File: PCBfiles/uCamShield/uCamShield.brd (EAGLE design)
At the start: 81.5 x 53.3 mm, 9 parts

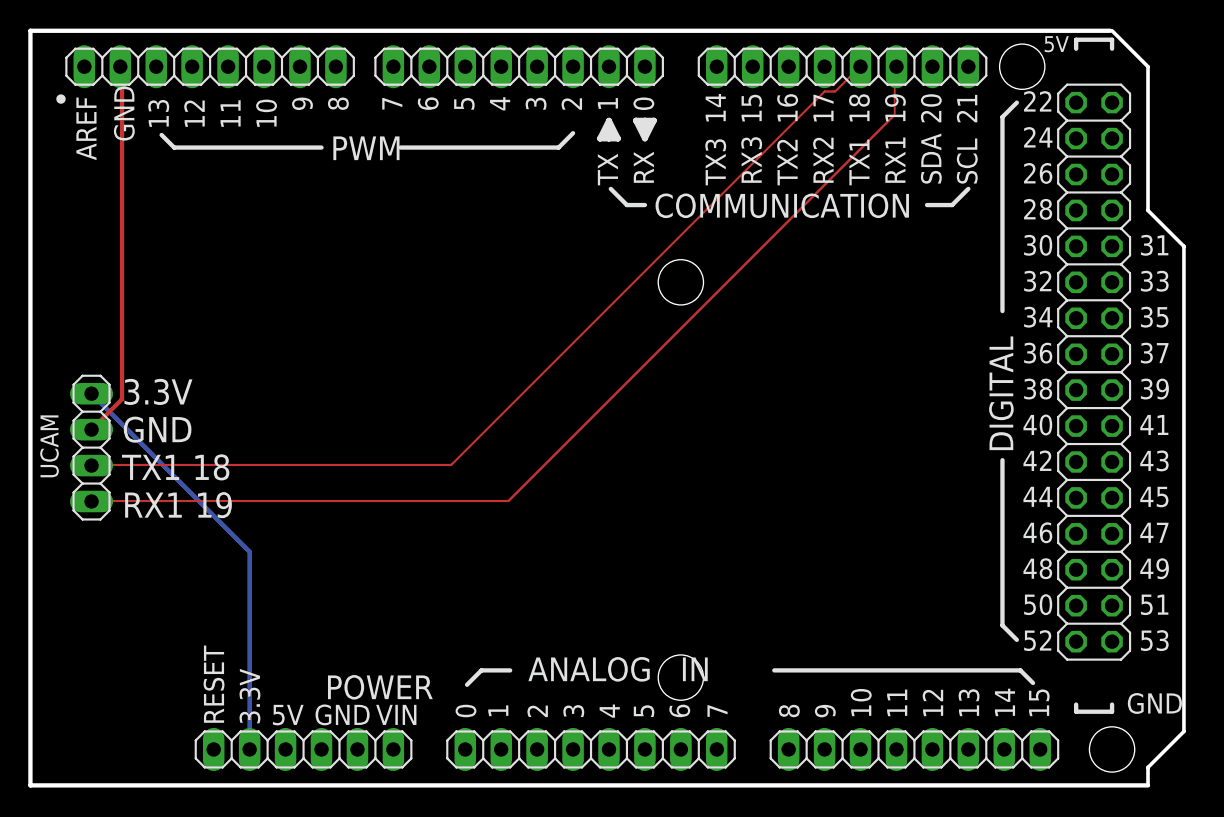
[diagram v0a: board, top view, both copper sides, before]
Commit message: Fixed PCB file for uCam shield
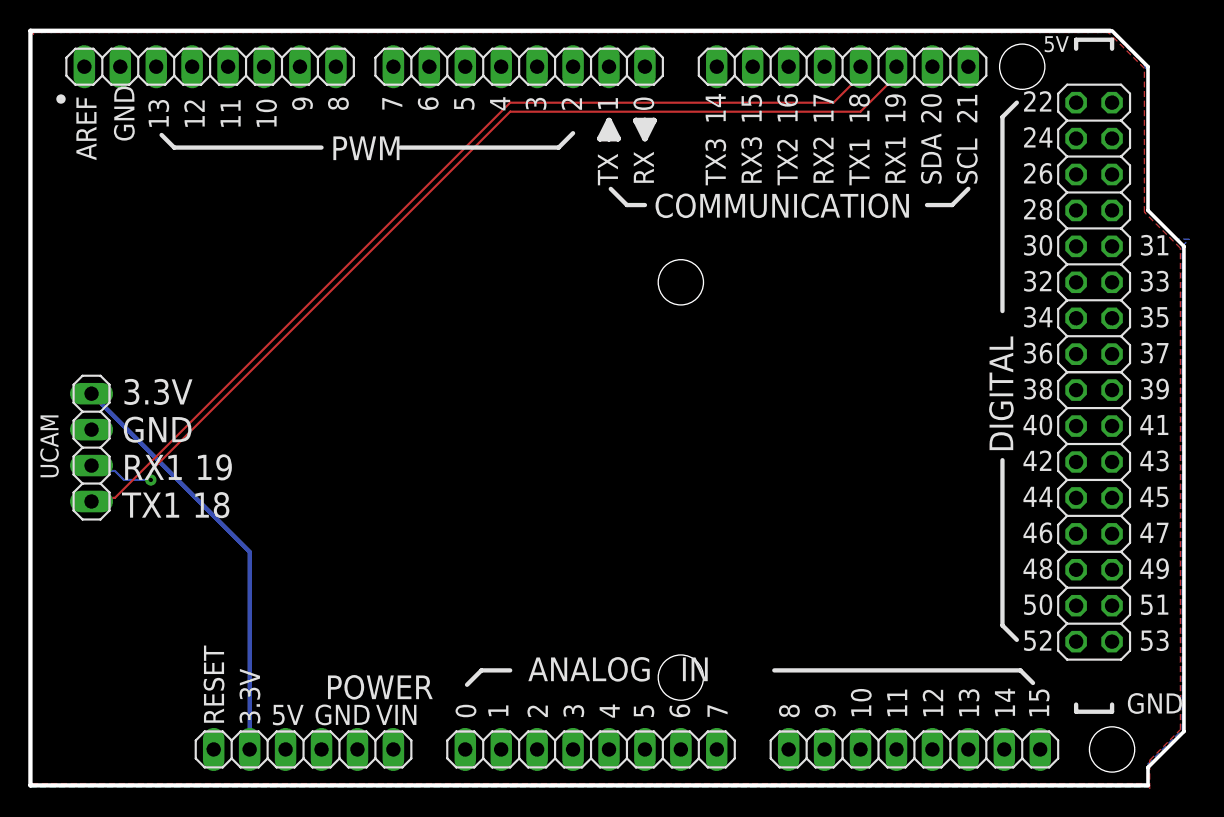
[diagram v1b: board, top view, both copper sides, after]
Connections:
- removed net N$4: COMMUNICATION.3, UCAM.1
- new net GND: POWER.4, POWER.5, PWMH.7, UCAM.3
- net N$2: now also COMMUNICATION.4, UCAM.1; no longer PWMH.7, UCAM.3
- net N$3: now also COMMUNICATION.3; no longer COMMUNICATION.4
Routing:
- net N$4: track 71.5 -> 0.00 mm
- net N$2: track 26.6 -> 67.4 mm
- net N$3: track 66.0 -> 70.2 mm, vias 0 -> 1
- added copper zone on layer 1, net GND
- added copper zone on layer 16, net GND
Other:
- board text added: "3.3V GND RX1 19 TX1 18"
- board text added: "uCAM-ARD-SHD rev0.2"
- board text removed: "3.3V GND TX1 18 RX1 19"
- board text removed: "uCAM-ARD-SHD rev.1"
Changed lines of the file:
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@@
 <text x="26.543" y="18.923" size="1.778" layer="21">3.3V
 GND
-TX1 18
-RX1 19</text>
+RX1 19
+TX1 18</text>
 <wire x1="96.393" y1="53.34" x2="20.066" y2="53.34" width="0.3048" layer="20"/>
 <wire x1="20.066" y1="53.34" x2="20.066" y2="0" width="0.3048" layer="20"/>
 <wire x1="20.066" y1="0" x2="99.06" y2="0" width="0.3048" layer="20"/>
 <text x="81.915" y="24.257" size="1.778" layer="22" rot="MR0">uCAM-ARD-SHD
-rev.1</text>
+rev0.2</text>
+<polygon width="0.4064" layer="22">
+<vertex x="43.688" y="31.242"/>
+<vertex x="41.021" y="31.242"/>
+<vertex x="38.227" y="28.448"/>
+<vertex x="38.227" y="19.558"/>
+<vertex x="39.878" y="19.558"/>
+<vertex x="40.005" y="19.685"/>
+<vertex x="40.005" y="27.94"/>
+<vertex x="41.656" y="29.591"/>
+<vertex x="43.815" y="29.591"/>
+<vertex x="45.212" y="28.194"/>
+<vertex x="45.212" y="19.558"/>
+<vertex x="45.085" y="19.431"/>
+<vertex x="47.117" y="19.431"/>
+<vertex x="47.117" y="28.067"/>
+<vertex x="44.069" y="31.115"/>
+</polygon>
+<polygon width="0.4064" layer="22">
+<vertex x="40.259" y="25.273"/>
+<vertex x="44.958" y="25.273"/>
+<vertex x="44.958" y="23.622"/>
+<vertex x="39.878" y="23.622"/>
+<vertex x="39.878" y="23.495"/>
+<vertex x="40.005" y="23.495"/>
+<vertex x="40.005" y="24.13"/>
+</polygon>
 </plain>
 <attributes>
@@
 <param name="RoutingGrid" value="50mil"/>
 <param name="AutoGrid" value="1"/>
-<param name="Efforts" value="0"/>
+<param name="Efforts" value="2"/>
 <param name="TopRouterVariant" value="1"/>
 <param name="tpViaShape" value="round"/>
-<param name="PrefDir.1" value="|"/>
+<param name="PrefDir.1" value="a"/>
 <param name="PrefDir.2" value="0"/>
 <param name="PrefDir.3" value="0"/>
@@
 <param name="PrefDir.14" value="0"/>
 <param name="PrefDir.15" value="0"/>
-<param name="PrefDir.16" value="-"/>
+<param name="PrefDir.16" value="a"/>
 <param name="cfVia" value="8"/>
 <param name="cfNonPref" value="5"/>
@@
 <wire x1="35.55" y1="3.45" x2="35.56" y2="3.556" width="0.15" layer="16"/>
 </signal>
+<signal name="GND">
+<contactref element="PWMH" pad="7"/>
+<contactref element="UCAM" pad="3"/>
+<contactref element="POWER" pad="4"/>
+<contactref element="POWER" pad="5"/>
+<polygon width="0.4064" layer="16">
+<vertex x="20.066" y="53.34"/>
+<vertex x="20.066" y="-0.127"/>
+<vertex x="98.933" y="-0.127"/>
+<vertex x="99.06" y="0"/>
+<vertex x="99.06" y="1.143"/>
+<vertex x="99.06" y="1.524"/>
+<vertex x="101.473" y="3.937"/>
+<vertex x="101.473" y="38.1"/>
+<vertex x="101.981" y="38.608"/>
+<vertex x="101.092" y="38.608"/>
+<vertex x="99.06" y="40.64"/>
+<vertex x="99.06" y="50.546"/>
+<vertex x="98.806" y="50.8"/>
+<vertex x="98.806" y="50.927"/>
+<vertex x="96.52" y="53.213"/>
+<vertex x="20.193" y="53.213"/>
+</polygon>
+<polygon width="0.4064" layer="1">
+<vertex x="20.066" y="53.213"/>
+<vertex x="20.066" y="0.254"/>
+<vertex x="20.193" y="0.127"/>
+<vertex x="98.806" y="0.127"/>
+<vertex x="99.187" y="-0.254"/>
+<vertex x="99.187" y="1.397"/>
+<vertex x="99.187" y="1.778"/>
+<vertex x="101.346" y="3.937"/>
+<vertex x="101.346" y="37.973"/>
+<vertex x="98.806" y="40.513"/>
+<vertex x="98.806" y="50.673"/>
+<vertex x="96.266" y="53.213"/>
+<vertex x="20.193" y="53.213"/>
+<vertex x="20.32" y="53.086"/>
+</polygon>
+</signal>
 <signal name="N$2">
-<contactref element="UCAM" pad="3"/>
-<contactref element="PWMH" pad="7"/>
-<wire x1="24.384" y1="25.146" x2="26.543" y2="27.305" width="0.3048" layer="1"/>
-<wire x1="26.543" y1="27.305" x2="26.543" y2="50.038" width="0.3048" layer="1"/>
-<wire x1="26.55" y1="50.1" x2="26.55" y2="50.7" width="0.15" layer="1"/>
-<wire x1="26.55" y1="50.7" x2="26.416" y2="50.8" width="0.15" layer="1"/>
-<wire x1="26.55" y1="50.1" x2="26.543" y2="50.038" width="0.15" layer="1"/>
+<contactref element="UCAM" pad="1"/>
+<contactref element="COMMUNICATION" pad="4"/>
+<wire x1="26.035" y1="20.32" x2="24.765" y2="20.32" width="0.15" layer="1"/>
+<wire x1="53.975" y1="48.26" x2="26.035" y2="20.32" width="0.15" layer="1"/>
+<wire x1="76.835" y1="48.26" x2="53.975" y2="48.26" width="0.15" layer="1"/>
+<wire x1="78.74" y1="50.165" x2="76.835" y2="48.26" width="0.15" layer="1"/>
+<wire x1="78.74" y1="50.8" x2="78.74" y2="50.165" width="0.15" layer="1"/>
+<wire x1="24.765" y1="20.32" x2="24.384" y2="20.066" width="0.15" layer="1"/>
 </signal>
 <signal name="N$3">
 <contactref element="UCAM" pad="2"/>
-<contactref element="COMMUNICATION" pad="4"/>
-<wire x1="49.8" y1="22.65" x2="24.45" y2="22.65" width="0.15" layer="1"/>
-<wire x1="76.2" y1="49.05" x2="49.8" y2="22.65" width="0.15" layer="1"/>
-<wire x1="76.95" y1="49.05" x2="76.2" y2="49.05" width="0.15" layer="1"/>
-<wire x1="78.6" y1="50.7" x2="76.95" y2="49.05" width="0.15" layer="1"/>
-<wire x1="24.45" y1="22.65" x2="24.384" y2="22.606" width="0.15" layer="1"/>
-<wire x1="78.6" y1="50.7" x2="78.74" y2="50.8" width="0.15" layer="1"/>
-</signal>
-<signal name="N$4">
-<contactref element="UCAM" pad="1"/>
 <contactref element="COMMUNICATION" pad="3"/>
-<wire x1="53.85" y1="20.1" x2="24.45" y2="20.1" width="0.15" layer="1"/>
-<wire x1="81.15" y1="47.4" x2="53.85" y2="20.1" width="0.15" layer="1"/>
-<wire x1="81.15" y1="50.7" x2="81.15" y2="47.4" width="0.15" layer="1"/>
-<wire x1="24.45" y1="20.1" x2="24.384" y2="20.066" width="0.15" layer="1"/>
-<wire x1="81.15" y1="50.7" x2="81.28" y2="50.8" width="0.15" layer="1"/>
+<wire x1="26.035" y1="22.225" x2="24.765" y2="22.225" width="0.15" layer="16"/>
+<wire x1="26.67" y1="21.59" x2="26.035" y2="22.225" width="0.15" layer="16"/>
+<wire x1="28.575" y1="21.59" x2="26.67" y2="21.59" width="0.15" layer="16"/>
+<wire x1="28.575" y1="22.225" x2="28.575" y2="21.59" width="0.15" layer="1"/>
+<wire x1="53.975" y1="47.625" x2="28.575" y2="22.225" width="0.15" layer="1"/>
+<wire x1="78.74" y1="47.625" x2="53.975" y2="47.625" width="0.15" layer="1"/>
+<wire x1="81.28" y1="50.165" x2="78.74" y2="47.625" width="0.15" layer="1"/>
+<wire x1="81.28" y1="50.8" x2="81.28" y2="50.165" width="0.15" layer="1"/>
+<wire x1="24.765" y1="22.225" x2="24.384" y2="22.606" width="0.15" layer="16"/>
+<via x="28.575" y="21.59" extent="1-16" drill="0.3"/>
 </signal>
 </signals>
